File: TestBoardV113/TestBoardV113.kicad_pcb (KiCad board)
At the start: 2 copper layers, 96 x 86 mm, 95 parts, among them J1 Conn_01x02_Socket, J10 Conn_01x02_Pin, J11 Conn_01x02_Pin, J12 Conn_01x02_Pin, J13 Conn_02x03_Odd_Even, J14 Conn_02x03_Odd_Even, J15 Conn_01x02_Pin, J16 Conn_02x03_Odd_Even, J17 Conn_01x01_Pin, J18 Conn_01x28_Socket, J19 Conn_01x01_Pin, J2 Conn_02x06_Odd_Even, J20 Conn_01x01_Pin, J21 Conn_01x02_Pin, J22 Conn_01x02_Socket, J23 Conn_01x28_Socket, J24 Conn_01x01_Pin, J25 Conn_01x02_Pin, J26 Conn_02x03_Odd_Even, J27 Conn_01x02_Pin, J28 Conn_01x02_Socket, J3 Conn_01x02_Pin, J4 Conn_01x02_Pin, J5 Conn_01x02_Pin, J6 Conn_01x02_Pin, J7 Conn_01x02_Pin, J8 Conn_01x02_Pin, J9 Conn_01x02_Pin, SW1 SW_DIP_x07, U3 NCP705MTADJTCG, U4 TAR5SxxU_SOT353F, U5 TXB0104PW, U6 TXB0104PW

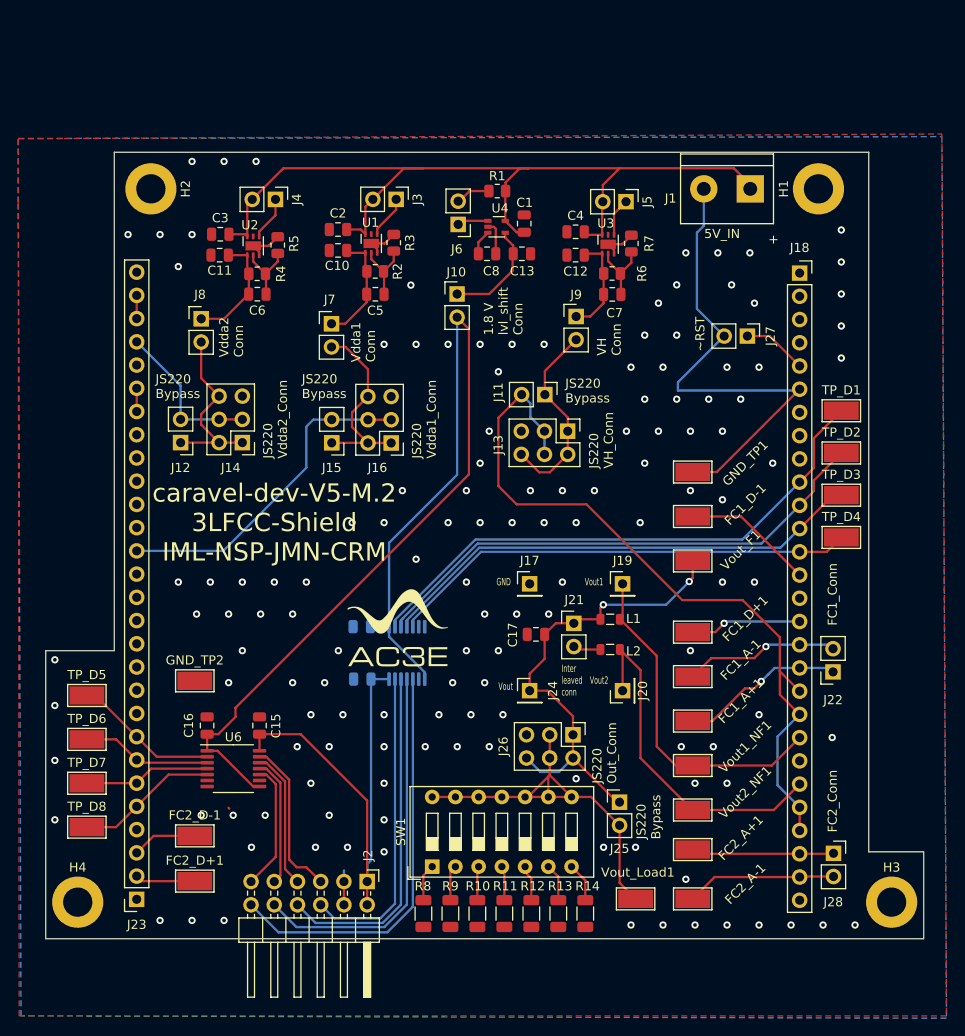
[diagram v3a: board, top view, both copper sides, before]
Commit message: Changes
Test Resistors from 0805 to 2010
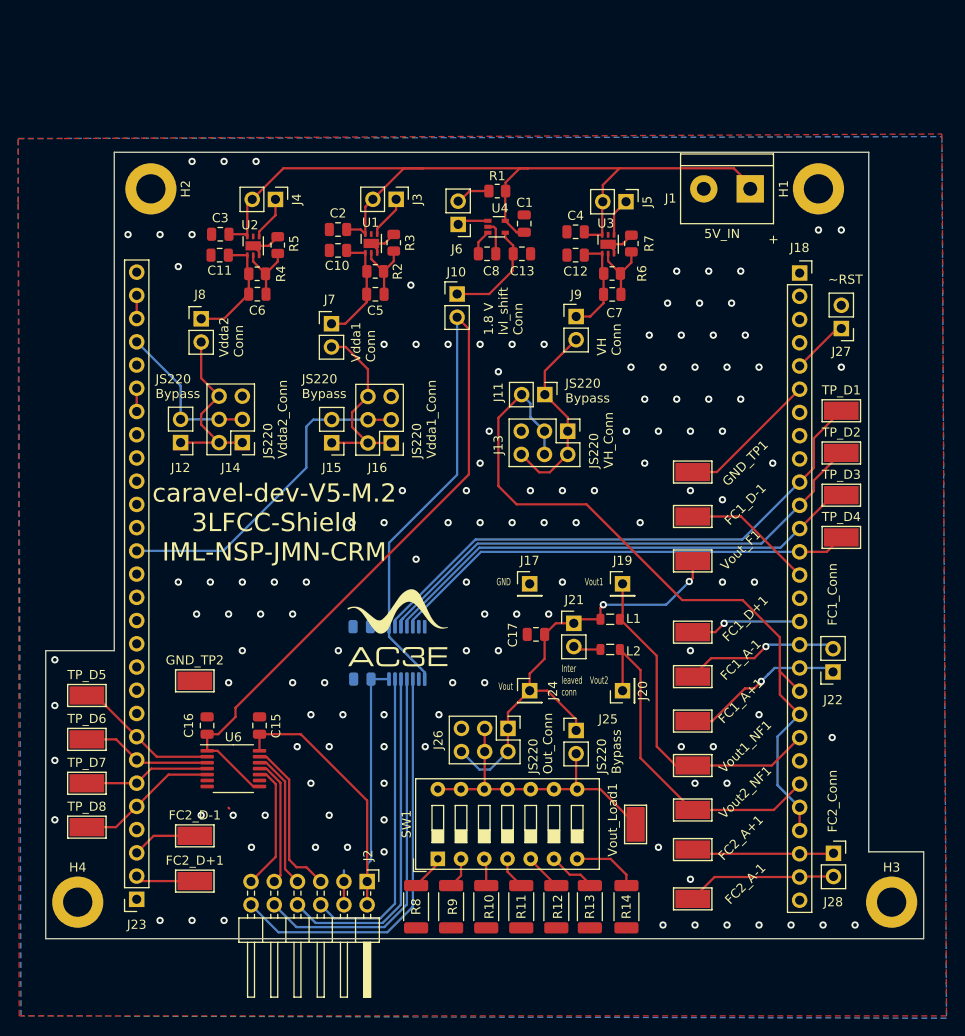
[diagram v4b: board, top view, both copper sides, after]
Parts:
- R10, R11, R12, R13, R14, R8, R9: footprint Resistor_SMD:R_1206_3216Metric -> Resistor_SMD:R_2010_5025Metric
- moved J27 10.3 mm to (183.0, 63.8), turned to 180 degrees
- moved J25 9.17 mm to (154.0, 107.7)
- moved Vout_Load1 8.14 mm to (160.5, 118.0), turned to 90 degrees
- moved J26 7.15 mm to (146.5, 107.5)
- moved R14 4.56 mm to (159.5, 127.0)
- moved R13 3.53 mm to (155.5, 127.0)
- moved R12 2.83 mm to (151.8, 127.0)
- moved R11 2.00 mm to (148.0, 127.0)
- moved R10 1.22 mm to (144.2, 127.0)
- moved R8 1.10 mm to (136.5, 127.0)
- moved SW1 1.05 mm to (138.9, 121.8)
- moved R9 0.75 mm to (140.3, 127.0)
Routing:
- net GND: track 74.9 -> 36.0 mm, vias 135 -> 128
- net Load conection +: track 44.5 -> 33.8 mm
- net Net-(R14-Pad1): track 4.29 -> 7.29 mm
- net Net-(J21-Pin_1): track 52.1 -> 50.1 mm
- net Net-(R13-Pad1): track 4.12 -> 5.30 mm
- net ~{RST}: track 7.07 -> 6.26 mm
- net Net-(R10-Pad1): track 3.73 -> 3.01 mm
- net Net-(R9-Pad1): track 3.90 -> 3.37 mm

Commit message: Changes
added real resistances values for the dip switch resistances and made the schematic more clear to read. Changed the fpga connector footprint for D1-D8 to avoid warnings
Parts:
- J2: footprint Connector_PinHeader_2.54mm:PinHeader_2x06_P2.54mm_Horizontal -> Connector_PinHeader_2.54mm:PinHeader_2x06_P2.54mm_Vertical
- moved G*** 14.7 mm to (120.0, 94.0)
- moved R1 0.26 mm to (145.4, 49.0)
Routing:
- net GND: vias 128 -> 130
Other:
- board text added: "1.8V EN"
- board text added: "VH EN"
- board text added: "Vdda1 EN"
- board text added: "Vdda2 EN"

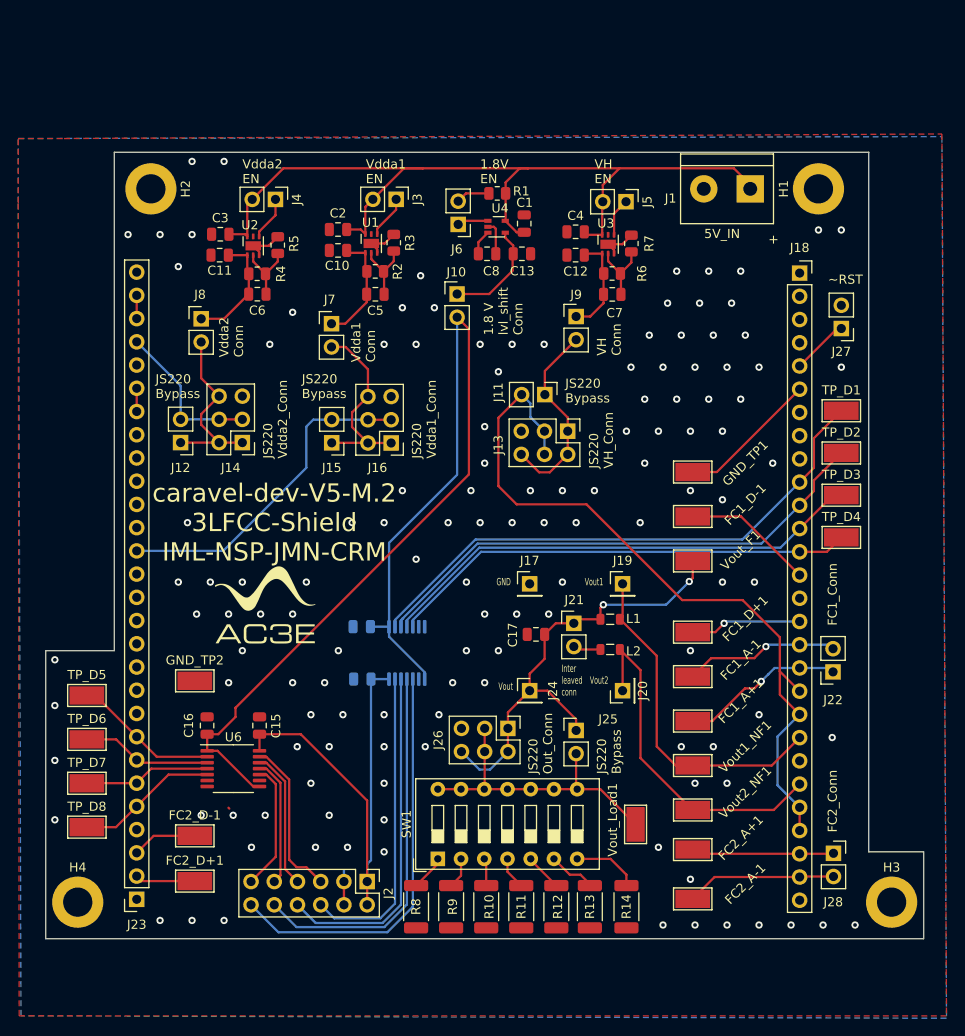
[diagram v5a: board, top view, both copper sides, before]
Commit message: Changes
increased tracks width, change some component placements for better dynamic response, added a connection to ground for vdda1, vdda2 and VH
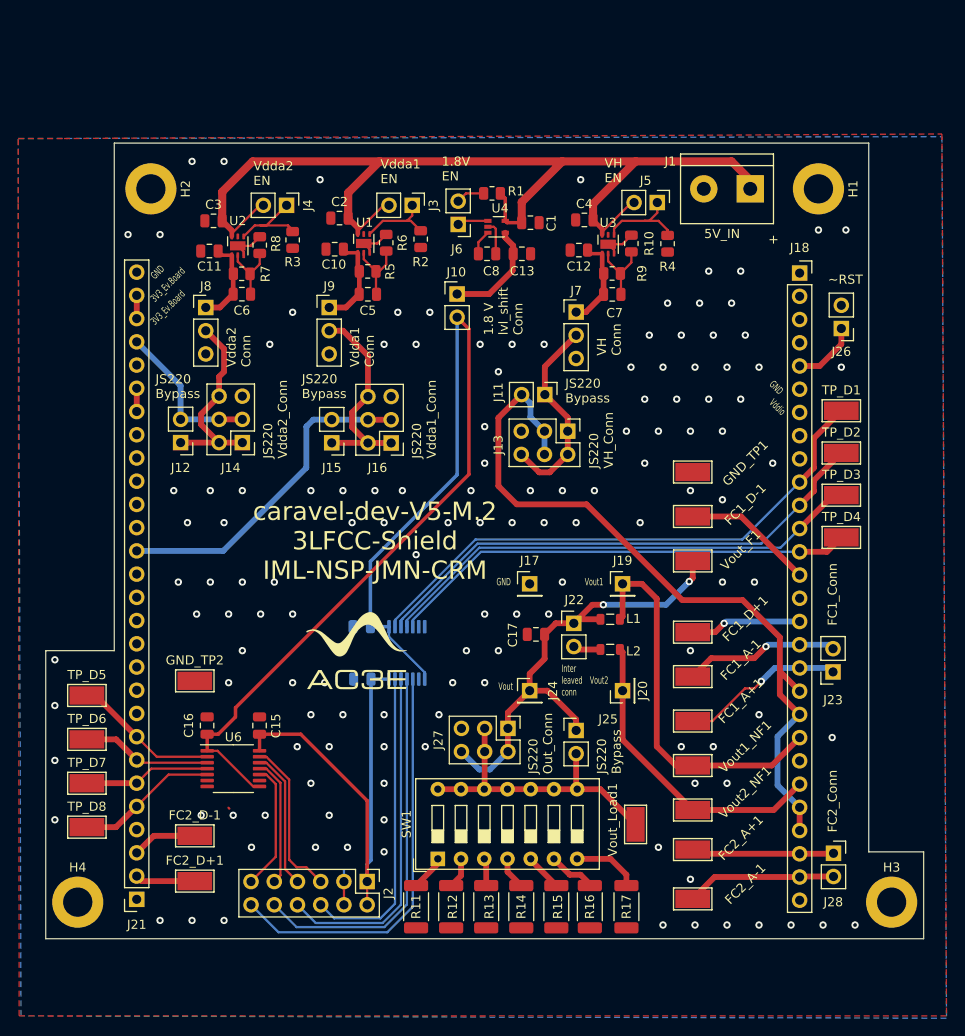
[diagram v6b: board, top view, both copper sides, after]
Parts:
- added R2: 100K, Resistor_SMD:R_0805_2012Metric, F.Cu at (137.0, 54.0)
- added R3: 100K, Resistor_SMD:R_0805_2012Metric, F.Cu at (123.0, 54.1)
- added R4: 100K, Resistor_SMD:R_0805_2012Metric, F.Cu at (164.0, 54.5)
- J7, J8, J9: value Conn_01x02_Pin -> Conn_01x03_Pin; footprint Connector_PinHeader_2.54mm:PinHeader_1x02_P2.54mm_Vertical -> Connector_PinHeader_2.54mm:PinHeader_1x03_P2.54mm_Vertical
- R11: renamed from R8; value 3K3 -> 3
- R12: renamed from R9; value 330 -> 3.6
- R13: renamed from R10; value 60 -> 4.5
- R14: renamed from R11; value 30 -> 6
- R15: renamed from R12; value 330 -> 9
- R16: renamed from R13; value 60 -> 18
- R17: renamed from R14; value 30 -> 36
- moved J9 27.0 mm to (127.0, 61.5)
- moved J7 26.8 mm to (154.0, 62.0)
- moved G*** 11.2 mm to (130.0, 99.0)
- moved J5 3.42 mm to (162.9, 50.0)
- moved R8 1.97 mm to (119.4, 54.7)
- moved J3 1.88 mm to (136.1, 50.3)
- moved C6 1.69 mm to (117.5, 60.0)
- moved U2 1.69 mm to (117.0, 54.7)
- moved R7 1.69 mm to (117.4, 57.8)
- moved C3 1.64 mm to (114.3, 52.0)
- moved C4 1.61 mm to (154.9, 51.9)
- moved J4 1.38 mm to (122.3, 50.3)
- moved J8 1.33 mm to (113.5, 61.5)
- moved C2 1.26 mm to (128.1, 51.7)
- moved C11 1.21 mm to (113.9, 55.3)
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- renumbered J23 to J21, J21 to J22, J22 to J23, J27 to J26, J26 to J27, R7 to R10, R2 to R5, R3 to R6, R4 to R7, R5 to R8, R6 to R9
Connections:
- C10 pad 1: Net-(J7-Pin_1) -> Net-(J9-Pin_1)
- C12 pad 1: Net-(J9-Pin_1) -> Net-(J7-Pin_1)
- C5 pad 1: Net-(J7-Pin_1) -> Net-(J9-Pin_1)
- C7 pad 1: Net-(J9-Pin_1) -> Net-(J7-Pin_1)
- J7 pad 2: Net-(J15-Pin_1) -> Net-(J11-Pin_1)
- J9 pad 2: Net-(J11-Pin_1) -> Net-(J15-Pin_1)
- R5 pad 1: Net-(J7-Pin_1) -> Net-(J9-Pin_1)
- R9 pad 1: Net-(J9-Pin_1) -> Net-(J7-Pin_1)
- U1 pad 1: Net-(J7-Pin_1) -> Net-(J9-Pin_1)
- U3 pad 1: Net-(J9-Pin_1) -> Net-(J7-Pin_1)
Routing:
- net VCC: track 97.2 -> 114.6 mm
- net GND: track 36.0 -> 20.3 mm, vias 130 -> 134
- net Net-(J5-Pin_1): track 4.16 -> 10.7 mm
- net Net-(J4-Pin_1): track 4.79 -> 9.98 mm
- net mprj_io[20]: track 37.4 -> 42.4 mm
- net mprj_io[18]: track 38.4 -> 33.8 mm
- net Net-(J3-Pin_1): track 4.65 -> 8.56 mm
- net Net-(J8-Pin_1): track 12.7 -> 9.63 mm
- net Net-(J7-Pin_1): track 12.7 -> 10.1 mm
- net Net-(J22-Pin_1): track 50.1 -> 52.5 mm
- net Net-(J15-Pin_1): track 21.0 -> 22.9 mm
- net Net-(J12-Pin_1): track 20.2 -> 21.7 mm
- net ~{RST}: track 6.26 -> 7.27 mm
- net Net-(J9-Pin_1): track 11.1 -> 10.2 mm
- net 1.8V-Shield: track 114.2 -> 115.0 mm
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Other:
- board size 96 x 86 mm -> 96 x 87 mm
- board text added: "3V3_Ev.Board"
- board text added: "Vddio"

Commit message: pull up for ~reset
Added pull-up resistor (100K) for ~Reset
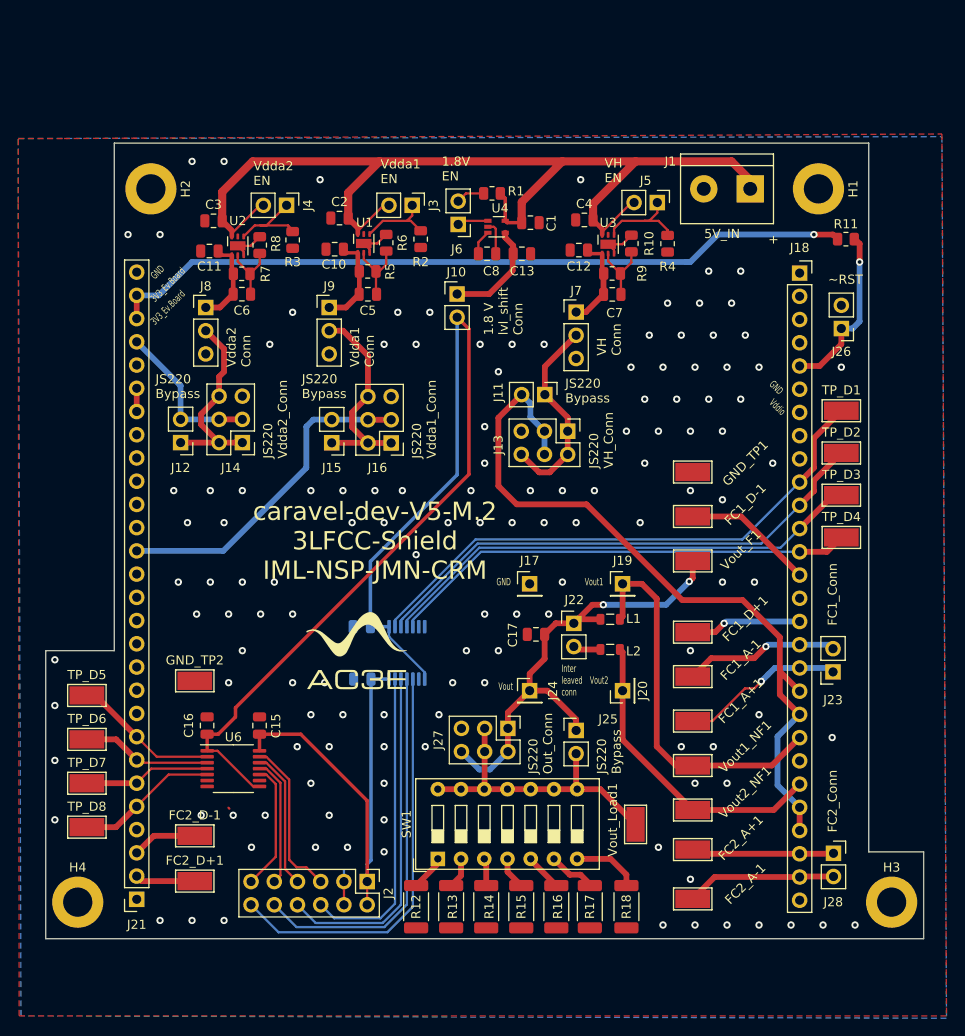
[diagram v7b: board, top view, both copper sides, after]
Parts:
- added R11: 100K, Resistor_SMD:R_0805_2012Metric, F.Cu at (183.5, 54.0)
- renumbered R11 to R12, R12 to R13, R13 to R14, R14 to R15, R15 to R16, R16 to R17, R17 to R18
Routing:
- net 3.3_EV_Board: track 2.54 -> 82.1 mm, vias 0 -> 1
- net ~{RST}: track 7.27 -> 18.9 mm, vias 0 -> 1
- net GND: vias 134 -> 132

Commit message: Changes
Added labels
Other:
- board size 96 x 87 mm -> 96 x 87.2 mm
- board text added: "IO[0]"
- board text added: "IO[14]"
- board text added: "IO[15]"
- board text added: "IO[1]"
- board text added: "IO[2]"
- board text added: "IO[34]"
- board text added: "IO[35]"
- board text added: "IO[36]"
- board text added: "IO[37]"
- board text added: "IO[3]"
- board text added: "IO[5]"
- board text added: "IO[6]"
- board text added: "IO[7]"
- board text added: "IO[8]"
- board text added: "IO[9]"
- board text added: "Vdda1"
- board text added: "Vdda2"
- board text added: "gpio"
- board text added: "xclk"
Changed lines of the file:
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@@
       (xy 192 130.5)
       (xy 192 121)
-      (xy 186 121)
-      (xy 186 43.5)
+      (xy 186.25 121)
+      (xy 186.25 43.25)
       (xy 103.5 43.5)
       (xy 103.5 99)
@@
     (effects (font (size 1 1) (thickness 0.15)) (justify left bottom))
   )
+  (gr_text "GND" (at 108 86.5 45) (layer "F.SilkS")
+    (effects (font (size 0.8 0.5) (thickness 0.125)) (justify left bottom))
+  )
   (gr_text "JS220\nBypass" (at 124 71.5) (layer "F.SilkS" knockout)
     (effects (font (size 1 1) (thickness 0.15)) (justify left bottom))
   )
+  (gr_text "IO[6]\n" (at 108 106.75 45) (layer "F.SilkS")
+    (effects (font (size 0.8 0.5) (thickness 0.125)) (justify left bottom))
+  )
+  (gr_text "IO[14]\n" (at 184.25 124.5 45) (layer "F.SilkS")
+    (effects (font (size 0.8 0.5) (thickness 0.125)) (justify left bottom))
+  )
+  (gr_text "IO[36]\n" (at 175 61.75 45) (layer "F.SilkS")
+    (effects (font (size 0.8 0.5) (thickness 0.125)) (justify left bottom))
+  )
+  (gr_text "IO[7]\n" (at 108 109.25 45) (layer "F.SilkS")
+    (effects (font (size 0.8 0.5) (thickness 0.125)) (justify left bottom))
+  )
+  (gr_text "GND" (at 108 84 45) (layer "F.SilkS")
+    (effects (font (size 0.8 0.5) (thickness 0.125)) (justify left bottom))
+  )
+  (gr_text "gpio" (at 108 79 45) (layer "F.SilkS")
+    (effects (font (size 0.8 0.5) (thickness 0.125)) (justify left bottom))
+  )
+  (gr_text "IO[5]\n" (at 108 104.25 45) (layer "F.SilkS")
+    (effects (font (size 0.8 0.5) (thickness 0.125)) (justify left bottom))
+  )
   (gr_text "VH\nConn" (at 159 66.75 90) (layer "F.SilkS" knockout)
     (effects (font (size 1 1) (thickness 0.15)) (justify left bottom))
@@
     (effects (font (size 1 1) (thickness 0.15)) (justify left bottom))
   )
+  (gr_text "IO[34]\n" (at 175 67 45) (layer "F.SilkS")
+    (effects (font (size 0.8 0.5) (thickness 0.125)) (justify left bottom))
+  )
+  (gr_text "IO[35]\n" (at 175 64.5 45) (layer "F.SilkS")
+    (effects (font (size 0.8 0.5) (thickness 0.125)) (justify left bottom))
+  )
   (gr_text "Vout2\n\n" (at 155.5 104) (layer "F.SilkS")
+    (effects (font (size 0.8 0.5) (thickness 0.125)) (justify left bottom))
+  )
+  (gr_text "Vdda1" (at 108 89 45) (layer "F.SilkS")
     (effects (font (size 0.8 0.5) (thickness 0.125)) (justify left bottom))
   )
@@
   (gr_text "Vdda1\nEN" (at 132.6 48) (layer "F.SilkS" knockout)
     (effects (font (size 1 1) (thickness 0.15)) (justify left bottom))
+  )
+  (gr_text "IO[0]\n" (at 108 91.5 45) (layer "F.SilkS")
+    (effects (font (size 0.8 0.5) (thickness 0.125)) (justify left bottom))
+  )
+  (gr_text "IO[37]\n" (at 175 59.25 45) (layer "F.SilkS")
+    (effects (font (size 0.8 0.5) (thickness 0.125)) (justify left bottom))
   )
   (gr_text "JS220\nVdda2_Conn" (at 122.5 78 90) (layer "F.SilkS" knockout)
@@
     (effects (font (size 1 1) (thickness 0.15)) (justify left bottom))
   )
+  (gr_text "GND\n" (at 175.75 127.5 45) (layer "F.SilkS")
+    (effects (font (size 0.8 0.5) (thickness 0.125)) (justify left bottom))
+  )
+  (gr_text "IO[8]\n" (at 108 111.75 45) (layer "F.SilkS")
+    (effects (font (size 0.8 0.5) (thickness 0.125)) (justify left bottom))
+  )
   (gr_text "1.8V\nEN" (at 139.3 47.7) (layer "F.SilkS" knockout)
     (effects (font (size 1 1) (thickness 0.15)) (justify left bottom))
@@
     (effects (font (size 1 1) (thickness 0.15)) (justify left bottom))
   )
-  (gr_text "Vddio" (at 175 72 315) (layer "F.SilkS")
+  (gr_text "Vddio" (at 175.5 74.25 45) (layer "F.SilkS")
     (effects (font (size 0.8 0.5) (thickness 0.125)) (justify left bottom))
   )
@@
     (effects (font (size 1 1) (thickness 0.15)) (justify left bottom))
   )
+  (gr_text "Vdda2" (at 108 66 45) (layer "F.SilkS")
+    (effects (font (size 0.8 0.5) (thickness 0.125)) (justify left bottom))
+  )
+  (gr_text "IO[15]\n" (at 184.25 122 45) (layer "F.SilkS")
+    (effects (font (size 0.8 0.5) (thickness 0.125)) (justify left bottom))
+  )
   (gr_text "FC1_Conn" (at 182.626 96.266 90) (layer "F.SilkS" knockout)
     (effects (font (size 1 1) (thickness 0.15)) (justify left bottom))
   )
+  (gr_text "GND" (at 108 127 45) (layer "F.SilkS")
+    (effects (font (size 0.8 0.5) (thickness 0.125)) (justify left bottom))
+  )
   (gr_text "JS220\nOut_Conn" (at 151.5 112.5 90) (layer "F.SilkS" knockout)
     (effects (font (size 1 1) (thickness 0.15)) (justify left bottom))
   )
+  (gr_text "IO[3]\n" (at 108 99 45) (layer "F.SilkS")
+    (effects (font (size 0.8 0.5) (thickness 0.125)) (justify left bottom))
+  )
   (gr_text "Vout\n" (at 145.5 103.378) (layer "F.SilkS")
     (effects (font (size 0.8 0.5) (thickness 0.125)) (justify left bottom))
@@
     (effects (font (size 1 1) (thickness 0.15)) (justify left bottom))
   )
+  (gr_text "IO[2]\n" (at 108 96.5 45) (layer "F.SilkS")
+    (effects (font (size 0.8 0.5) (thickness 0.125)) (justify left bottom))
+  )
   (gr_text "+\n" (at 175.006 54.61) (layer "F.SilkS")
     (effects (font (size 1 1) (thickness 0.15)) (justify left bottom))
   )
+  (gr_text "IO[9]\n" (at 108 114.25 45) (layer "F.SilkS")
+    (effects (font (size 0.8 0.5) (thickness 0.125)) (justify left bottom))
+  )
   (gr_text "Vdda2\nConn" (at 118.5 68 90) (layer "F.SilkS" knockout)
     (effects (font (size 1 1) (thickness 0.15)) (justify left bottom))
   )
-  (gr_text "GND\n" (at 175 70 315) (layer "F.SilkS")
+  (gr_text "~RST\n\n" (at 176.5 70.25 45) (layer "F.SilkS")
+    (effects (font (size 0.8 0.5) (thickness 0.125)) (justify left bottom))
+  )
+  (gr_text "GND\n" (at 176 71.5 45) (layer "F.SilkS")
     (effects (font (size 0.8 0.5) (thickness 0.125)) (justify left bottom))
   )
@@
     (effects (font (size 1 1) (thickness 0.15)) (justify left bottom))
   )
+  (gr_text "IO[1]\n" (at 108 94 45) (layer "F.SilkS")
+    (effects (font (size 0.8 0.5) (thickness 0.125)) (justify left bottom))
+  )
   (gr_text "JS220\nBypass" (at 159 112.5 90) (layer "F.SilkS" knockout)
     (effects (font (size 1 1) (thickness 0.15)) (justify left bottom))
   )
+  (gr_text "xclk" (at 108 81.5 45) (layer "F.SilkS")
+    (effects (font (size 0.8 0.5) (thickness 0.125)) (justify left bottom))
+  )
   (gr_text "Vout1\n" (at 154.94 91.948) (layer "F.SilkS")
